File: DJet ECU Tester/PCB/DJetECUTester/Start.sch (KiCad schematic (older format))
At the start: 6 parts, among them Q11 MMBT2222ALT1G, Q12 MMBT3906LT1G

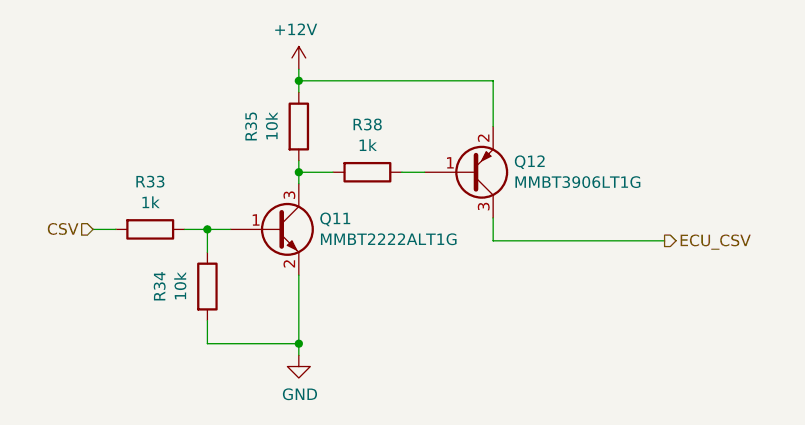
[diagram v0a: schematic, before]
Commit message: Renamed CSV to Start. Added PDF version of schematics.
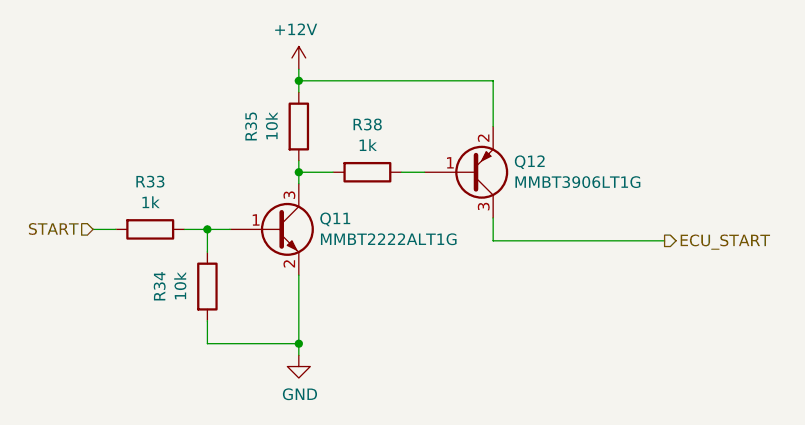
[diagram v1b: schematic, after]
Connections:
- net CSV renamed START
- net ECU_CSV renamed ECU_START
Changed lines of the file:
@@
 Sheet 7 7
 Title "D-Jetronic ECU Tester"
-Date "2021-03-15"
+Date "2021-03-20"
 Rev "1.0"
 Comp "(C) Britishideas 2021"
@@
 $EndDescr
 Text HLabel 6950 4150 2    50   Output ~ 0
-ECU_CSV
+ECU_START
 Text HLabel 4450 4100 0    50   Input ~ 0
-CSV
+START
 $Comp
 L Device:R R?
